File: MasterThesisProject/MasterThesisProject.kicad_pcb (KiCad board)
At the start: 2 copper layers, 227.1 x 129.8 mm, 45 parts, among them J1 Conn_01x07_Male, J2 Barrel_Jack, SW1 SW_MEC_5E, U1 LCD_I2C, U10 TGS5342, U11 CDM7160, U12 INA128, U13 LM4041AILT-1.2, U14 LPS331PA_Module, U2 SensironSPS30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

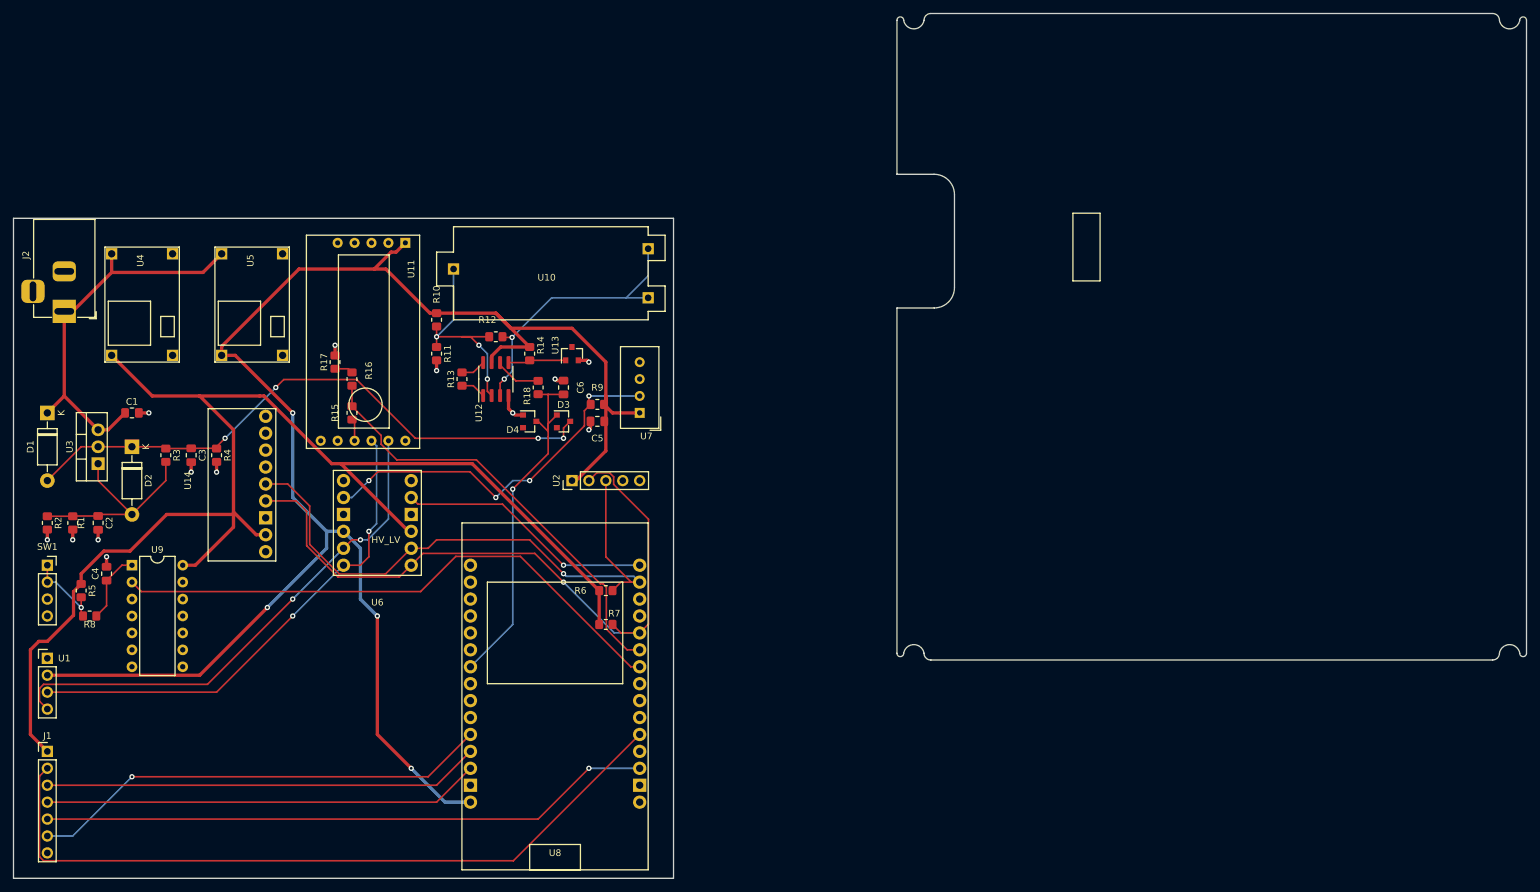
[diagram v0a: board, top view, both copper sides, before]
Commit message: Update W5500 schematic and PCB to match custom PCB connectino
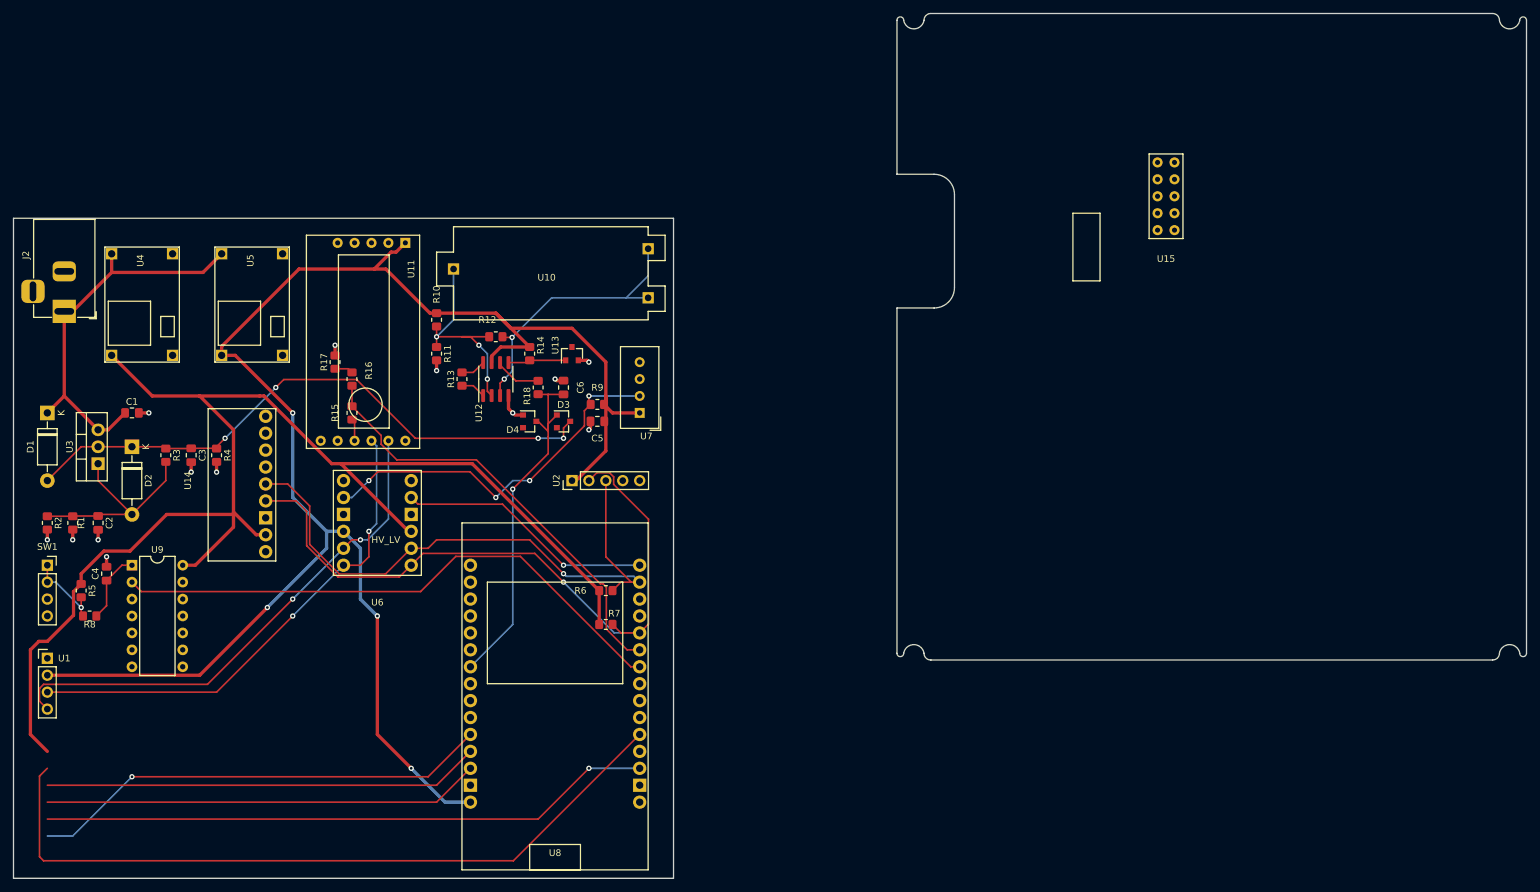
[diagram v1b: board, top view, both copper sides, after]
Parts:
- removed J1: Conn_01x07_Male, Connector_PinHeader_2.54mm:PinHeader_1x07_P2.54mm_Vertical
- added U15: W5500_SPI_ETH, CustomFootprints:W5500_SPI_ETH, F.Cu at (211.1, 71.6)
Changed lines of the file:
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@@
     (zones 0)
     (modules 45)
-    (nets 70)
+    (nets 73)
   )
   (page A4)
@@
   (net 68 "Net-(U6-Pad1)")
   (net 69 "Net-(U6-Pad7)")
+  (net 70 "Net-(U15-Pad6)")
+  (net 71 "Net-(U15-Pad8)")
+  (net 72 "Net-(U15-Pad10)")
   (net_class Default "This is the default net class."
     (clearance 0.2)
@@
     (add_net "Net-(U14-Pad8)")
     (add_net "Net-(U14-Pad9)")
+    (add_net "Net-(U15-Pad10)")
+    (add_net "Net-(U15-Pad6)")
+    (add_net "Net-(U15-Pad8)")
     (add_net "Net-(U6-Pad1)")
     (add_net "Net-(U6-Pad7)")
@@
       (net 7 CO_SENSOR))
     (model ${KISYS3DMOD}/Diode_SMD.3dshapes/D_SOT-23.wrl
-      (at (xyz 0 0 0))
-      (scale (xyz 1 1 1))
-      (rotate (xyz 0 0 0))
-    )
-  )
-  (module Connector_PinHeader_2.54mm:PinHeader_1x07_P2.54mm_Vertical (layer F.Cu)
-    (at 43.18 146.05)
-    (descr "Through hole straight pin header, 1x07, 2.54mm pitch, single row")
-    (tags "Through hole pin header THT 1x07 2.54mm single row")
-    (fp_text reference J1 (at 0 -2.33) (layer F.SilkS)
-      (effects (font (size 1 1) (thickness 0.15)))
-    )
-    (fp_text value Conn_01x07_Male (at 0 17.57) (layer F.Fab)
-      (effects (font (size 1 1) (thickness 0.15)))
-    )
-    (fp_line (start 1.8 -1.8) (end -1.8 -1.8) (layer F.CrtYd) (width 0.05))
-    (fp_line (start 1.8 17.05) (end 1.8 -1.8) (layer F.CrtYd) (width 0.05))
-    (fp_line (start -1.8 17.05) (end 1.8 17.05) (layer F.CrtYd) (width 0.05))
-    (fp_line (start -1.8 -1.8) (end -1.8 17.05) (layer F.CrtYd) (width 0.05))
-    (fp_line (start -1.33 -1.33) (end 0 -1.33) (layer F.SilkS) (width 0.12))
-    (fp_line (start -1.33 0) (end -1.33 -1.33) (layer F.SilkS) (width 0.12))
-    (fp_line (start -1.33 1.27) (end 1.33 1.27) (layer F.SilkS) (width 0.12))
-    (fp_line (start 1.33 1.27) (end 1.33 16.57) (layer F.SilkS) (width 0.12))
-    (fp_line (start -1.33 1.27) (end -1.33 16.57) (layer F.SilkS) (width 0.12))
-    (fp_line (start -1.33 16.57) (end 1.33 16.57) (layer F.SilkS) (width 0.12))
-    (fp_line (start -1.27 -0.635) (end -0.635 -1.27) (layer F.Fab) (width 0.1))
-    (fp_line (start -1.27 16.51) (end -1.27 -0.635) (layer F.Fab) (width 0.1))
-    (fp_line (start 1.27 16.51) (end -1.27 16.51) (layer F.Fab) (width 0.1))
-    (fp_line (start 1.27 -1.27) (end 1.27 16.51) (layer F.Fab) (width 0.1))
-    (fp_line (start -0.635 -1.27) (end 1.27 -1.27) (layer F.Fab) (width 0.1))
-    (fp_text user %R (at 0 7.62 90) (layer F.Fab)
-      (effects (font (size 1 1) (thickness 0.15)))
-    )
-    (pad 1 thru_hole rect (at 0 0) (size 1.7 1.7) (drill 1) (layers *.Cu *.Mask)
-      (net 8 +3V3))
-    (pad 2 thru_hole oval (at 0 2.54) (size 1.7 1.7) (drill 1) (layers *.Cu *.Mask)
-      (net 9 ETH_INT))
-    (pad 3 thru_hole oval (at 0 5.08) (size 1.7 1.7) (drill 1) (layers *.Cu *.Mask)
-      (net 10 SPI_MISO))
-    (pad 4 thru_hole oval (at 0 7.62) (size 1.7 1.7) (drill 1) (layers *.Cu *.Mask)
-      (net 11 SPI_MOSI))
-    (pad 5 thru_hole oval (at 0 10.16) (size 1.7 1.7) (drill 1) (layers *.Cu *.Mask)
-      (net 12 SPI_CS))
-    (pad 6 thru_hole oval (at 0 12.7) (size 1.7 1.7) (drill 1) (layers *.Cu *.Mask)
-      (net 13 SPI_CLK))
-    (pad 7 thru_hole oval (at 0 15.24) (size 1.7 1.7) (drill 1) (layers *.Cu *.Mask)
-      (net 2 GND))
-    (model ${KISYS3DMOD}/Connector_PinHeader_2.54mm.3dshapes/PinHeader_1x07_P2.54mm_Vertical.wrl
       (at (xyz 0 0 0))
       (scale (xyz 1 1 1))
@@
       (rotate (xyz 0 0 0))
     )
+  )
+  (module CustomFootprints:W5500_SPI_ETH (layer F.Cu)
+    (at 211.074 71.628)
+    (fp_text reference U15 (at 0 0.5) (layer F.SilkS)
+      (effects (font (size 1 1) (thickness 0.15)))
+    )
+    (fp_text value W5500_SPI_ETH (at 0 -0.5) (layer F.Fab)
+      (effects (font (size 1 1) (thickness 0.15)))
+    )
+    (fp_line (start -2.54 -2.54) (end -2.54 -15.24) (layer F.SilkS) (width 0.12))
+    (fp_line (start 2.54 -2.54) (end -2.54 -2.54) (layer F.SilkS) (width 0.12))
+    (fp_line (start 2.54 -15.24) (end 2.54 -2.54) (layer F.SilkS) (width 0.12))
+    (fp_line (start -2.54 -15.24) (end 2.54 -15.24) (layer F.SilkS) (width 0.12))
+    (pad 1 thru_hole circle (at -1.27 -13.97) (size 1.524 1.524) (drill 0.762) (layers *.Cu *.Mask)
+      (net 8 +3V3))
+    (pad 2 thru_hole circle (at -1.27 -11.43) (size 1.524 1.524) (drill 0.762) (layers *.Cu *.Mask)
+      (net 10 SPI_MISO))
+    (pad 3 thru_hole circle (at -1.27 -8.89) (size 1.524 1.524) (drill 0.762) (layers *.Cu *.Mask)
+      (net 11 SPI_MOSI))
+    (pad 4 thru_hole circle (at -1.27 -6.35) (size 1.524 1.524) (drill 0.762) (layers *.Cu *.Mask)
+      (net 12 SPI_CS))
+    (pad 5 thru_hole circle (at -1.27 -3.81) (size 1.524 1.524) (drill 0.762) (layers *.Cu *.Mask)
+      (net 13 SPI_CLK))
+    (pad 6 thru_hole circle (at 1.27 -13.97) (size 1.524 1.524) (drill 0.762) (layers *.Cu *.Mask)
+      (net 70 "Net-(U15-Pad6)"))
+    (pad 7 thru_hole circle (at 1.27 -11.43) (size 1.524 1.524) (drill 0.762) (layers *.Cu *.Mask)
+      (net 2 GND))
+    (pad 8 thru_hole circle (at 1.27 -8.89) (size 1.524 1.524) (drill 0.762) (layers *.Cu *.Mask)
+      (net 71 "Net-(U15-Pad8)"))
+    (pad 9 thru_hole circle (at 1.27 -6.35) (size 1.524 1.524) (drill 0.762) (layers *.Cu *.Mask)
+      (net 9 ETH_INT))
+    (pad 10 thru_hole circle (at 1.27 -3.81) (size 1.524 1.524) (drill 0.762) (layers *.Cu *.Mask)
+      (net 72 "Net-(U15-Pad10)"))
   )
   (gr_line (start 197.104 75.438) (end 197.104 65.278) (layer F.SilkS) (width 0.12))
@@
   (segment (start 127 87.63) (end 127 92.71) (width 0.5) (layer F.Cu) (net 6))
   (segment (start 127 92.71) (end 127 93.71) (width 0.5) (layer F.Cu) (net 6) (status 20))
-  (segment (start 85.09 113.03) (end 87.63 113.03) (width 0.5) (layer B.Cu) (net 6))
+  (segment (start 85.09 113.03) (end 87.63 113.03) (width 0.5) (layer B.Cu) (net 6) (status 20))
   (segment (start 80.01 107.95) (end 85.09 113.03) (width 0.5) (layer B.Cu) (net 6))
   (segment (start 80.01 95.25) (end 80.01 107.95) (width 0.5) (layer B.Cu) (net 6))
@@
   (segment (start 71.12 110.126213) (end 71.12 110.49) (width 0.5) (layer F.Cu) (net 8))
   (segment (start 71.12 110.49) (end 71.12 112.38) (width 0.5) (layer F.Cu) (net 8))
-  (segment (start 40.64 143.51) (end 43.18 146.05) (width 0.5) (layer F.Cu) (net 8) (status 20))
+  (segment (start 40.64 143.51) (end 43.18 146.05) (width 0.5) (layer F.Cu) (net 8))
   (segment (start 47.10999 125.61001) (end 43.18 129.54) (width 0.5) (layer F.Cu) (net 8))
   (segment (start 47.10999 122.07001) (end 47.10999 125.61001) (width 0.5) (layer F.Cu) (net 8))
@@
   (segment (start 42.004999 161.854001) (end 42.615999 162.465001) (width 0.25) (layer F.Cu) (net 9))
   (segment (start 42.004999 149.765001) (end 42.004999 161.854001) (width 0.25) (layer F.Cu) (net 9))
-  (segment (start 43.18 148.59) (end 42.004999 149.765001) (width 0.25) (layer F.Cu) (net 9) (status 10))
+  (segment (start 43.18 148.59) (end 42.004999 149.765001) (width 0.25) (layer F.Cu) (net 9))
   (segment (start 101.6 151.13) (end 106.68 146.05) (width 0.25) (layer F.Cu) (net 10) (status 20))
-  (segment (start 43.18 151.13) (end 101.6 151.13) (width 0.25) (layer F.Cu) (net 10) (status 10))
+  (segment (start 43.18 151.13) (end 101.6 151.13) (width 0.25) (layer F.Cu) (net 10))
   (segment (start 101.6 153.67) (end 106.68 148.59) (width 0.25) (layer F.Cu) (net 11) (status 20))
-  (segment (start 43.18 153.67) (end 101.6 153.67) (width 0.25) (layer F.Cu) (net 11) (status 10))
+  (segment (start 43.18 153.67) (end 101.6 153.67) (width 0.25) (layer F.Cu) (net 11))
   (segment (start 116.84 156.21) (end 124.46 148.59) (width 0.25) (layer F.Cu) (net 12))
   (via (at 124.46 148.59) (size 0.8) (drill 0.4) (layers F.Cu B.Cu) (net 12))
-  (segment (start 43.18 156.21) (end 116.84 156.21) (width 0.25) (layer F.Cu) (net 12) (status 10))
+  (segment (start 43.18 156.21) (end 116.84 156.21) (width 0.25) (layer F.Cu) (net 12))
   (segment (start 124.46 148.59) (end 132.08 148.59) (width 0.25) (layer B.Cu) (net 12) (status 20))
-  (segment (start 43.18 158.75) (end 46.99 158.75) (width 0.25) (layer B.Cu) (net 13) (status 10))
+  (segment (start 43.18 158.75) (end 46.99 158.75) (width 0.25) (layer B.Cu) (net 13))
   (segment (start 46.99 158.75) (end 55.88 149.86) (width 0.25) (layer B.Cu) (net 13))
   (via (at 55.88 149.86) (size 0.8) (drill 0.4) (layers F.Cu B.Cu) (net 13))

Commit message: Remove old pcb, port elements to new one
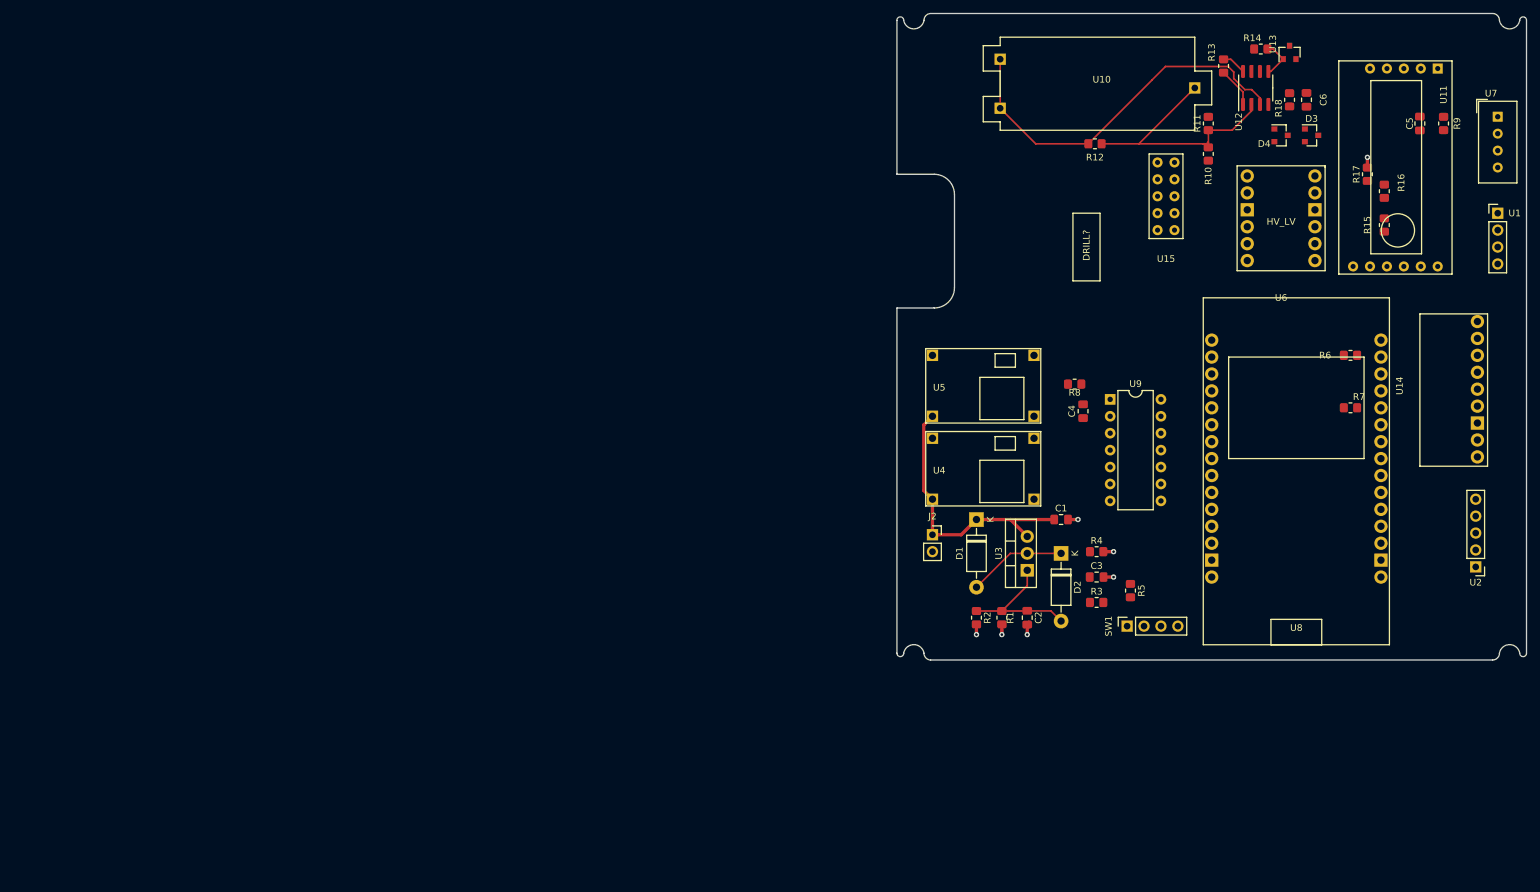
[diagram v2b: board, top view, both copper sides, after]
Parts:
- J2: footprint Connector_BarrelJack:BarrelJack_Horizontal -> Connector_PinSocket_2.54mm:PinSocket_1x02_P2.54mm_Vertical
- moved U1 227.7 mm to (260.9, 65.3)
- moved U14 182.4 mm to (246.6, 91.2)
- moved SW1 162.3 mm to (205.2, 127.3), turned to 90 degrees
- moved R15 157.5 mm to (243.8, 67.1)
- moved R16 157.5 mm to (243.8, 62.0)
- moved R17 157.5 mm to (241.3, 59.4)
- moved R5 157.5 mm to (205.7, 121.9)
- moved U11 157.1 mm to (254.0, 42.4)
- moved R8 151.9 mm to (197.4, 90.9)
- moved U9 148.9 mm to (202.7, 93.2)
- moved C4 148.6 mm to (198.6, 95.0)
- moved U6 143.1 mm to (228.3, 77.5)
- moved R3 141.4 mm to (200.7, 123.7), turned to 0 degrees
- moved U3 140.4 mm to (190.2, 118.9)
- moved C1 140.4 mm to (195.3, 111.3)
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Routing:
- net +5V: track 257.9 -> 0.00 mm, vias 4 -> 0
- net +3V3: track 203.8 -> 0.00 mm
- net ETH_INT: track 111.9 -> 0.00 mm
- net SDA: track 105.5 -> 0.00 mm, vias 1 -> 0
- net SPI_CS: track 92.1 -> 0.00 mm, vias 1 -> 0
- net SCL: track 91.3 -> 0.00 mm, vias 1 -> 0
- net LCD_BUTTON: track 85.8 -> 0.00 mm
- net SCL_HIGH: track 78.2 -> 0.00 mm, vias 2 -> 0
- net +3V0: track 90.8 -> 15.2 mm, vias 4 -> 0
- net SDA_HIGH: track 74.9 -> 0.00 mm, vias 2 -> 0
- net SPI_CLK: track 69.8 -> 0.00 mm, vias 1 -> 0
- net CO2_BUSY: track 65.9 -> 0.00 mm
- net SPI_MOSI: track 65.6 -> 0.00 mm
- net SPI_MISO: track 65.6 -> 0.00 mm
- net DHT_HIGH: track 56.4 -> 0.00 mm, vias 4 -> 0
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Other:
- board size 227.1 x 129.8 mm -> 94.5 x 97 mm
- board text added: "DRILL?"
